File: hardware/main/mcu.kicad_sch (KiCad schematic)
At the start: 15 parts, among them SW101 Reset, SW102 Boot, U101 ESP32-A1S

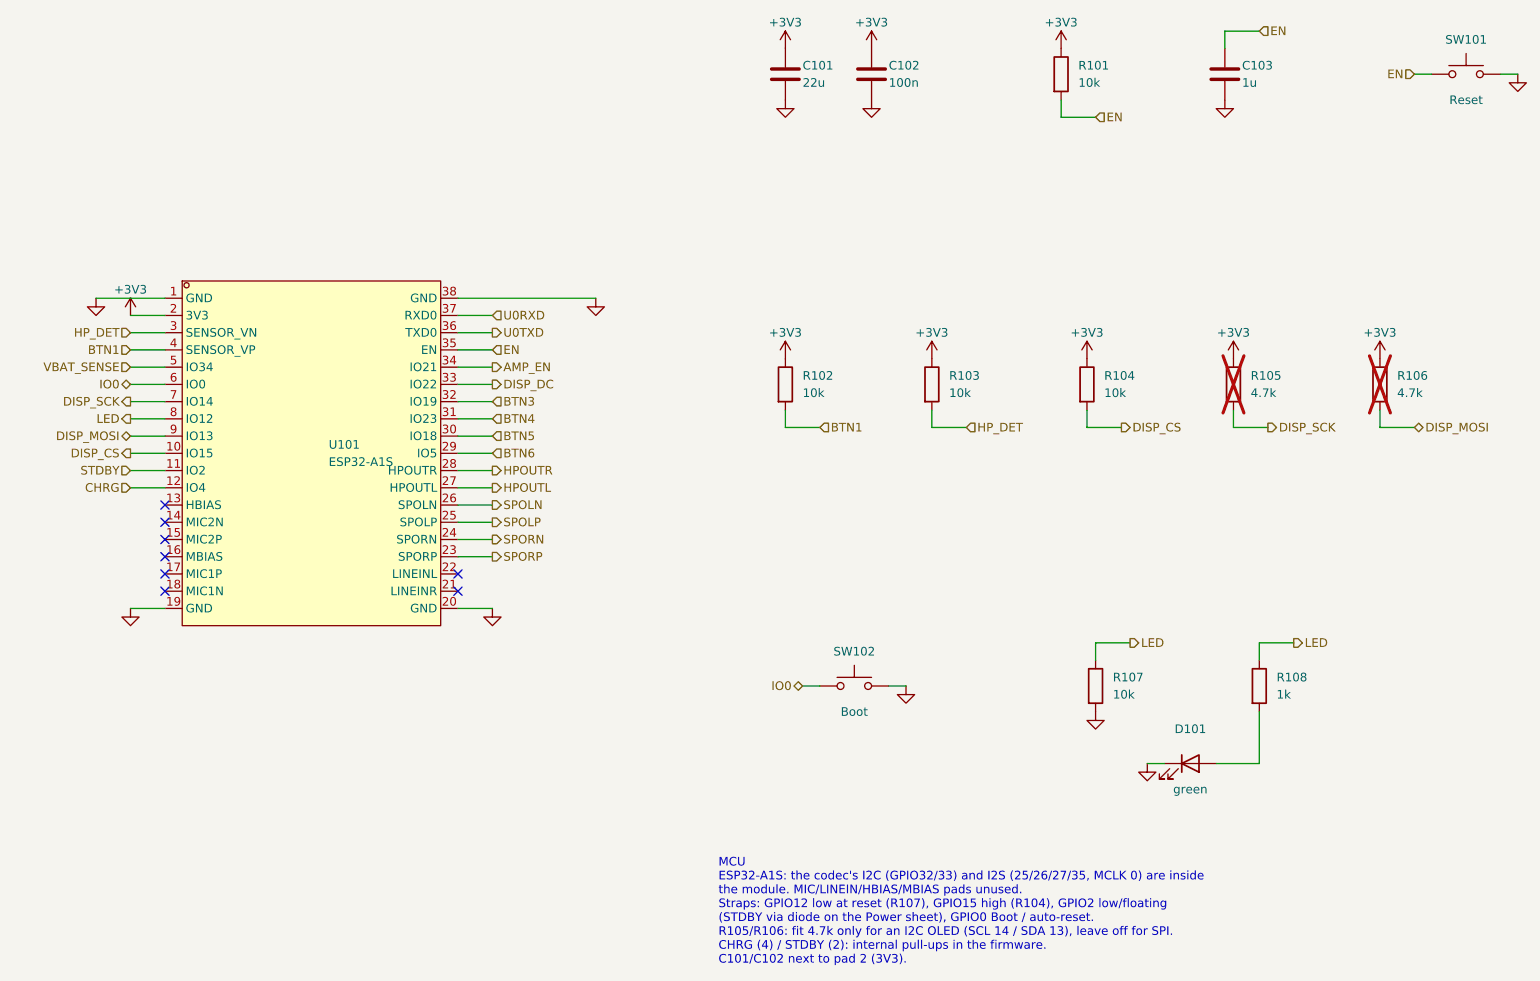
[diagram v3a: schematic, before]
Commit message: hardware: headphone jack removed, main board 70 x 60 mm
- J403, C422, C423 out; HPOUTL/R open, GPIO39 spare with its pull-up.
- Main board re-placed on 70 x 60 mm (decoupling placed first), routed,
  labelled; route.py cleans dangling vias and sub-minimum tracks.
- LCSC fields rewritten after regenerating MCU and Audio sheets.

Co-Authored-By: Claude Opus 5.5 <noreply@anthropic.com>
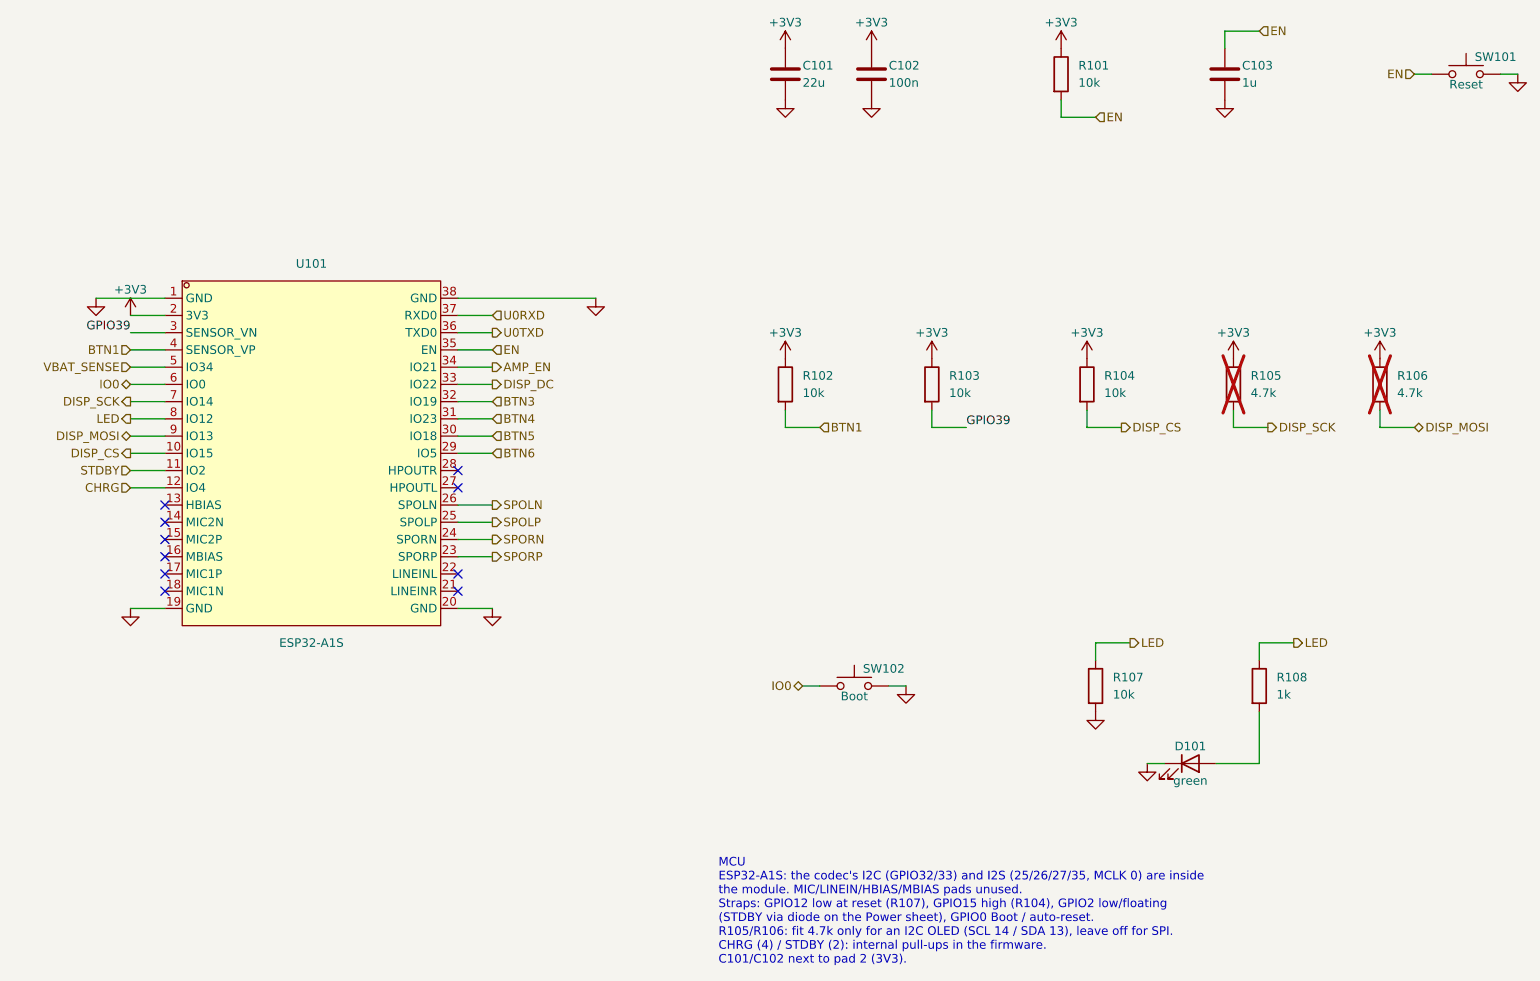
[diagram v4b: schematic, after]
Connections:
- net HPOUTL: no longer names the net of U101.27 (HPOUTL)
- net HPOUTR: no longer names the net of U101.28 (HPOUTR)
- net HP_DET renamed GPIO39
- no-connect marks 8 -> 10
